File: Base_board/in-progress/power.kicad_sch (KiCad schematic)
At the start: 45 parts, among them J13 Wire pad, J14 Wire pad, J15 Wire pad, J16 Wire pad, J5 Conn_01x02, J9 USB_A, Q6 2N7002, SW3 SW_Push, U3 MCP16331T-E/CH, U4 BTS50080-1TEA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

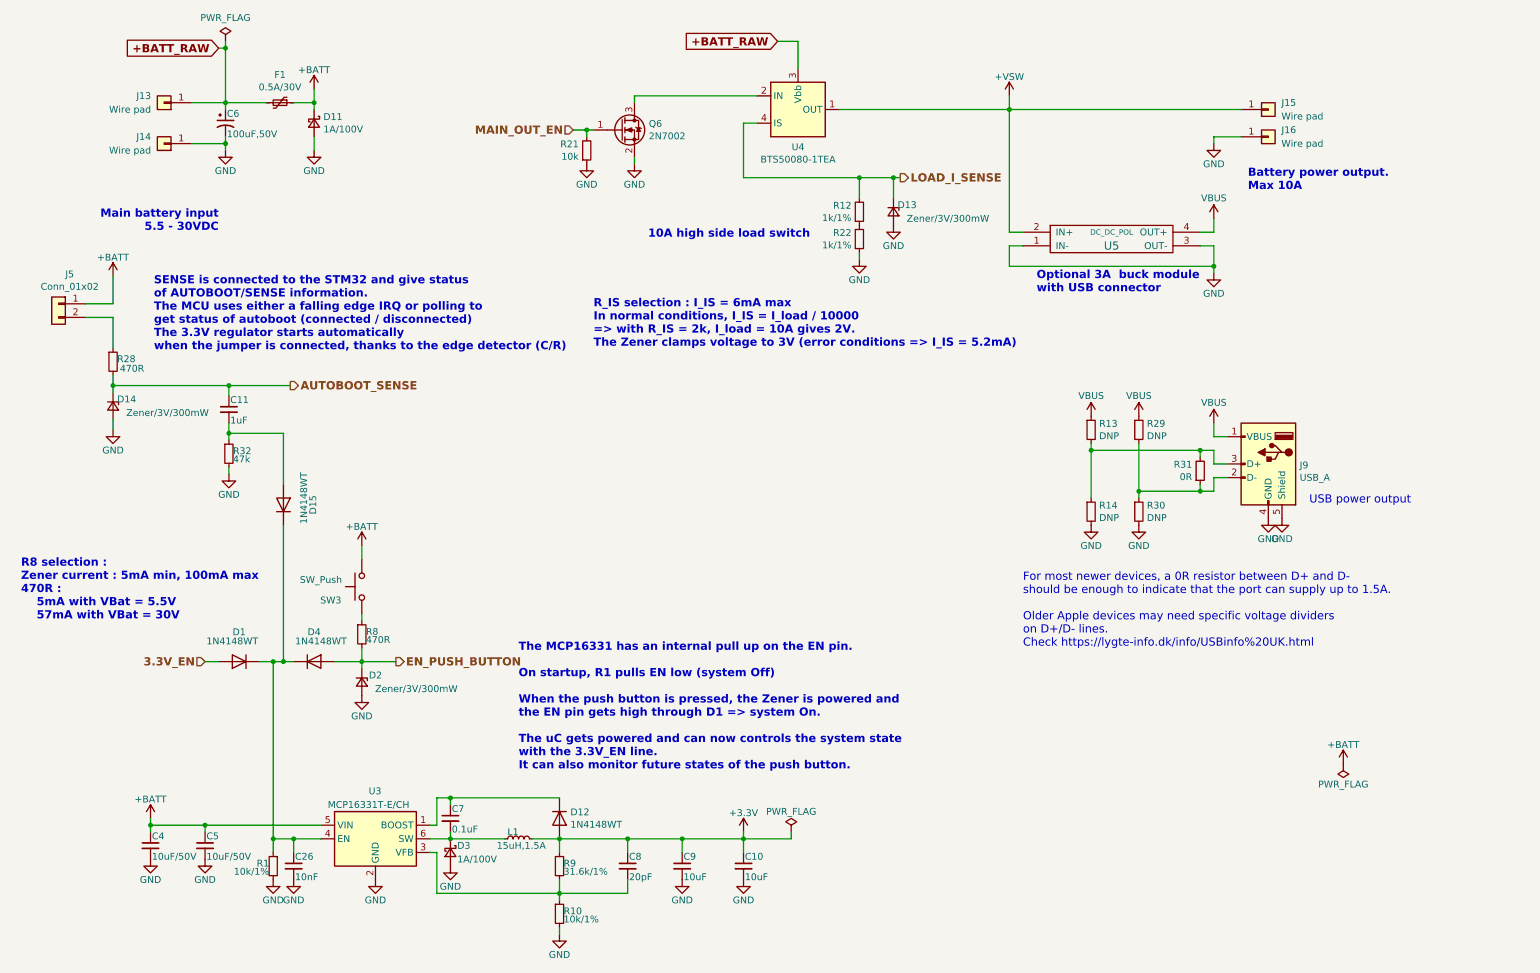
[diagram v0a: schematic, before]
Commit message: update v3.2
-  connecteur XT60 coudé (et disponible chez JLCPCB)
- modification de l’autoboot pour un redémarrage en cas de perte brêve d’alimentation,
- ajout de l’empreinte pour rajouter une lecteur microSD
- mise à jour des piste de sortie batterie conforme pour 10A
- suppression des pin I2C (déjà dispo sur le GPIO)
- connecteur JST B3B-EH pour un câblage et éviter les soudure qui casse sur les sortie pour LED
- ESP32 en version 16M
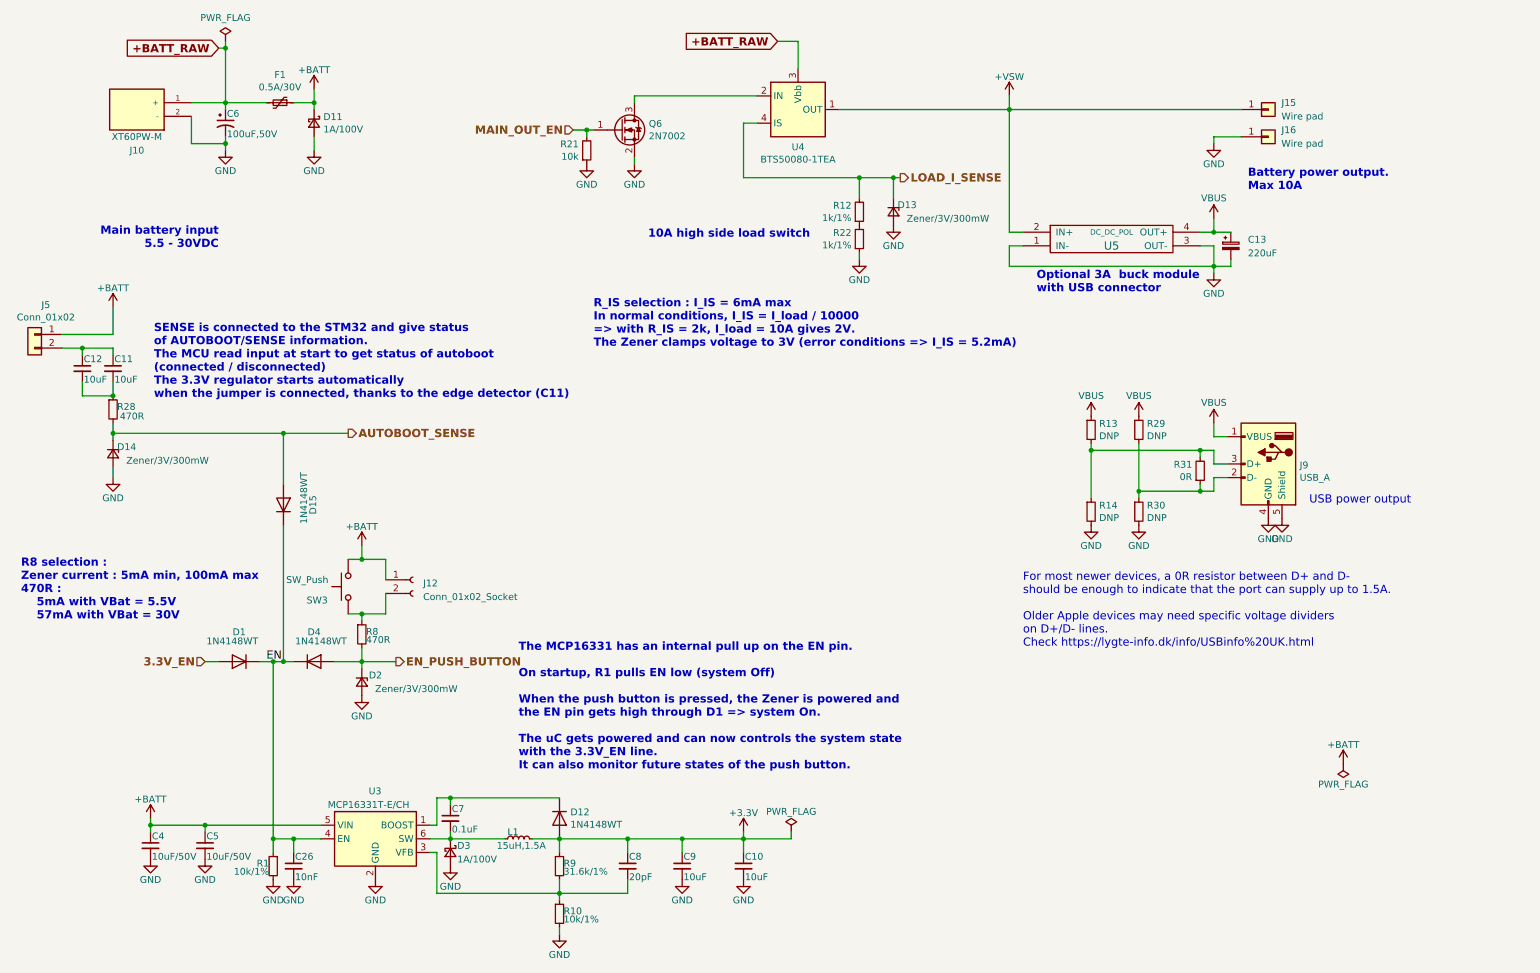
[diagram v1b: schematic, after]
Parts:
- removed J13, J14: Wire pad, Connector_Wire:SolderWirePad_1x01_Drill2mm, symbol Connector_Generic:Conn_01x01
- removed R32: 47k, Resistor_SMD:R_0603_1608Metric, symbol Device:R_Small
- added C12: 10uF, Capacitor_SMD:C_0805_2012Metric, symbol Device:C_Small
- added C13: 220uF, Capacitor_THT:CP_Radial_D5.0mm_P2.50mm, symbol Device:C_Polarized_Small
- added J10: XT60PW-M, XT60PW-M:AMASS_XT60PW-M, symbol XT60PW-M:XT60PW-M
- added J12: Conn_01x02_Socket, Connector_PinHeader_2.54mm:PinHeader_1x02_P2.54mm_Vertical, symbol Connector:Conn_01x02_Socket
- C11: value 1uF -> 10uF; footprint Capacitor_SMD:C_0603_1608Metric -> Capacitor_SMD:C_0805_2012Metric
- C26: LCSC (none) -> C57112
- C4, C5: LCSC (none) -> C13585
- C6: LCSC (none) -> C97812
- C7: LCSC (none) -> C14663
- C8: LCSC (none) -> C1648
- D1, D12, D15, D4: LCSC (none) -> C68948
- D11, D3: LCSC (none) -> C14996
- D13, D14, D2: LCSC (none) -> C19869
- F1: LCSC (none) -> C2924945
- J9: LCSC (none) -> C2345
- L1: LCSC (none) -> C206232
- Q6: LCSC (none) -> C8545
- R1, R10, R21: LCSC (none) -> C25804
- R12, R22: LCSC (none) -> C21190
- R28, R8: LCSC (none) -> C23179
- R31: LCSC (none) -> C21189
- R9: LCSC (none) -> C25967
- SW3: footprint tom_kicad_lib:SW_Tactile_SPST_Angled_PTS645Vx58-2LFS_horiz_pads -> Button_Switch_THT:SW_Tactile_SPST_Angled_PTS645Vx31-2LFS; LCSC (none) -> C127680
- U3: LCSC (none) -> C105695
- U4: LCSC (none) -> C152393
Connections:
- net +BATT: now also J12.1 (Pin_1)
- net +BATT_RAW: now also J10.1 (+)
- net AUTOBOOT_SENSE: now also D15.2 (A); no longer C11.1
- net GND: now also C13.2, J10.2 (-)
- net VBUS: now also C13.1
- net EN: now reaches C26.1, D1.1 (K), D15.1 (K), D4.1 (K), R1.1, U3.4 (EN)
- net at R8.1, SW3.1: now also J12.2 (Pin_2)
- net at R28.1: now also C11.2, C12.2; no longer J5.2 (Pin_2)
- new net: C11.1, C12.1, J5.2 (Pin_2)
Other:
- note added: "SENSE is connected to the STM32 and give status of AUTOBOOT/SENSE information. The MCU read input at start to get status of autoboot (connected / disconnected) The 3.3V regulator starts automatically when the jumper is connected, thanks to the edge detector (C11)"
- note removed: "SENSE is connected to the STM32 and give status of AUTOBOOT/SENSE information. The MCU uses either a falling edge IRQ or polling to get status of autoboot (connected / disconnected) The 3.3V regulator starts automatically when the jumper is connected, thanks to the edge detector (C/R)"
- title: (none) -> ESP32 battery management module
- moved on the sheet: C11, D14, J5, R28, SW3

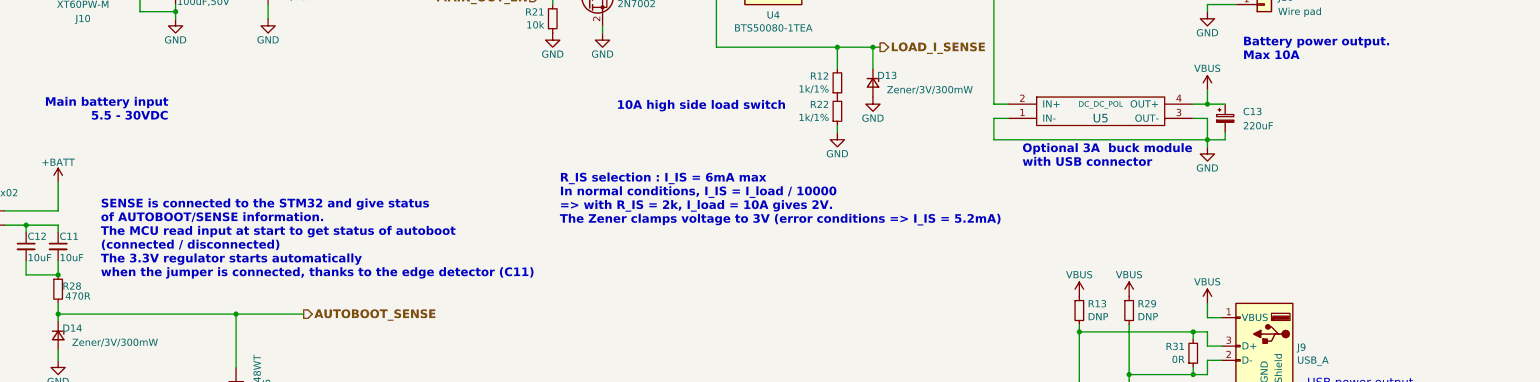
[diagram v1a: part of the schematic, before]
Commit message: update to v3.2 and casing 3D View
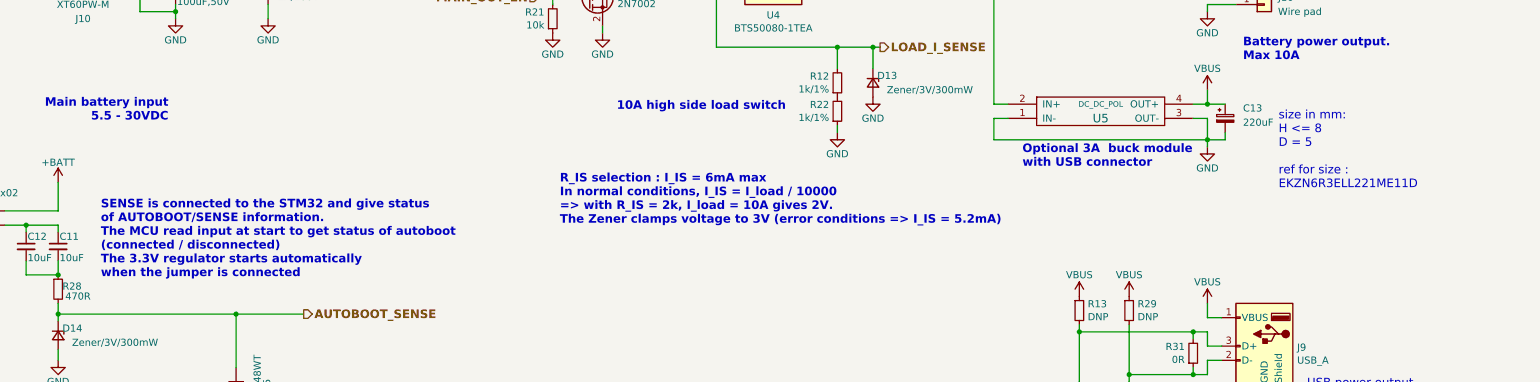
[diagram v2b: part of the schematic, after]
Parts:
- C13: footprint Capacitor_THT:CP_Radial_D5.0mm_P2.50mm -> Capacitor_THT:CP_Radial_D5.0mm_P2.00mm; LCSC (none) -> C2977547
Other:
- note added: "SENSE is connected to the STM32 and give status of AUTOBOOT/SENSE information. The MCU read input at start to get status of autoboot (connected / disconnected) The 3.3V regulator starts automatically when the jumper is connected"
- note added: "size in mm: H <= 8 D = 5 ref for size : EKZN6R3ELL221ME11D"
- note removed: "SENSE is connected to the STM32 and give status of AUTOBOOT/SENSE information. The MCU read input at start to get status of autoboot (connected / disconnected) The 3.3V regulator starts automatically when the jumper is connected, thanks to the edge detector (C11)"
- company: (none) -> for : KXKM
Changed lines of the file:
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@@
     (date "2023-06-14")
     (rev "3.2")
-    (comment 1 "Tom Magnier / initial release")
-    (comment 2 "Viven Henry / SD, Switch, Autoboot")
-    (comment 3 "Clément SAILLANT / update Autoboot, readd SD")
+    (company "for : KXKM")
+    (comment 1 "update PCB, add optional SD, ....")
+    (comment 2 "Clément SAILLANT (v3.2) : improve Autoboot")
+    (comment 3 "Viven Henry (v3) : remove SD, add Switch, add Autoboot")
+    (comment 4 "Tom Magnier :  initial release (v1 & v2)")
   )
   (junction (at 224.79 106.68) (diameter 0) (color 0 0 0 0)
@@
     (effects (font (size 1.524 1.524) (thickness 0.3048) bold) (justify left bottom))
   )
+  (text "size in mm:\nH <= 8\nD = 5\n\nref for size :\nEKZN6R3ELL221ME11D\n"
+    (at 251.46 73.66 0)
+    (effects (font (size 1.524 1.524)) (justify left bottom))
+  )
   (text "10A high side load switch" (at 133.35 59.69 0)
     (effects (font (size 1.524 1.524) (thickness 0.3048) bold) (justify left bottom))
@@
     (effects (font (size 1.524 1.524)) (justify left bottom))
   )
-  (text "SENSE is connected to the STM32 and give status \nof AUTOBOOT/SENSE information.\nThe MCU read input at start to get status of autoboot\n(connected / disconnected)\nThe 3.3V regulator starts automatically  \nwhen the jumper is connected, thanks to the edge detector (C11)\n"
+  (text "SENSE is connected to the STM32 and give status \nof AUTOBOOT/SENSE information.\nThe MCU read input at start to get status of autoboot\n(connected / disconnected)\nThe 3.3V regulator starts automatically  \nwhen the jumper is connected"
     (at 41.275 89.535 0)
     (effects (font (size 1.524 1.524) (thickness 0.3048) bold) (justify left bottom))
@@
   (symbol (lib_id "Device:C_Polarized_Small") (at 241.935 60.96 0) (unit 1)
     (in_bom yes) (on_board yes) (dnp no) (fields_autoplaced)
-    (property "Reference" "C13" (at 245.11 59.7789 0)
-      (effects (font (size 1.27 1.27)) (justify left))
-    )
-    (property "Value" "220uF" (at 245.11 62.3189 0)
-      (effects (font (size 1.27 1.27)) (justify left))
-    )
-    (property "Footprint" "Capacitor_THT:CP_Radial_D5.0mm_P2.50mm" (at 241.935 60.96 0)
-      (effects (font (size 1.27 1.27)) hide)
-    )
-    (property "Datasheet" "~" (at 241.935 60.96 0)
-      (effects (font (size 1.27 1.27)) hide)
-    )
-    (property "LCSC" "" (at 241.935 60.96 0)
-      (effects (font (size 1.27 1.27)) hide)
-    )
+    (property "Reference" "C13" (at 245.11 59.1439 0)
+      (effects (font (size 1.27 1.27)) (justify left))
+    )
+    (property "Value" "220uF" (at 245.11 61.6839 0)
+      (effects (font (size 1.27 1.27)) (justify left))
+    )
+    (property "Footprint" "Capacitor_THT:CP_Radial_D5.0mm_P2.00mm" (at 241.935 60.96 0)
+      (effects (font (size 1.27 1.27)) hide)
+    )
+    (property "Datasheet" "EKZN6R3ELL221ME11D" (at 241.935 60.96 0)
+      (effects (font (size 1.27 1.27)) hide)
+    )
+    (property "LCSC" "C2977547" (at 241.935 60.96 0)
+      (effects (font (size 1.27 1.27)) hide)
+    )
